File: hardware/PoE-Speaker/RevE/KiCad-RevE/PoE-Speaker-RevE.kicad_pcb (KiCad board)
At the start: 4 copper layers, 210 x 100 mm, 209 parts, among them J1 2250506-1, J2 MX2EDGR-5.08-02P-GN01-Cu-A, J3 MX2EDGR-5.08-02P-GN01-Cu-A, J4 Pin Header 02x07 2.54mm Verti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, J5 Pin Header 01x06 2.54mm Verti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, J6 Pin Header 01x06 2.54mm Verti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, Q1 DMNH6012LK3-13, Q2 DMNH6012LK3-13, Q3 PSMN4R8-100BSE, Q4 PSMN4R8-100BSE, SW1 TS-1088-AR02016, SW2 TS-1088-AR02016, U1 Ag5800, U10 LM5050-2, U11 PCAL6416APW, U12 PC817X2NSZ9F, U13 PC817X2NSZ9F, U14 PC817X2NSZ9F, U15 LTC4365HTS8#TRPBF, U16 TPS26630RGER, U2 ESP32-S3-WROOM-1U-N16R8, U3 W5500, U4 PCM5122PWR, U5 TPA3116D2, U6 LMR33630AQRNXRQ1, U7 TPS62132RGTR, U8 RT9013-33GB, U9 LM5050-2, X2 25MHz

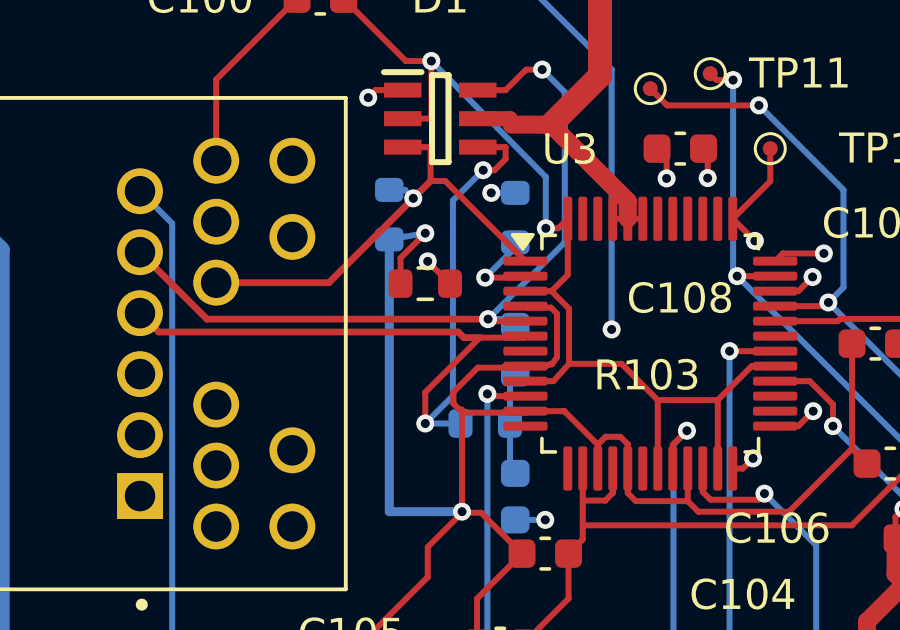
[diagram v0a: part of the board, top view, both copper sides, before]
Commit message: Shorten RX positive branch routing for #1
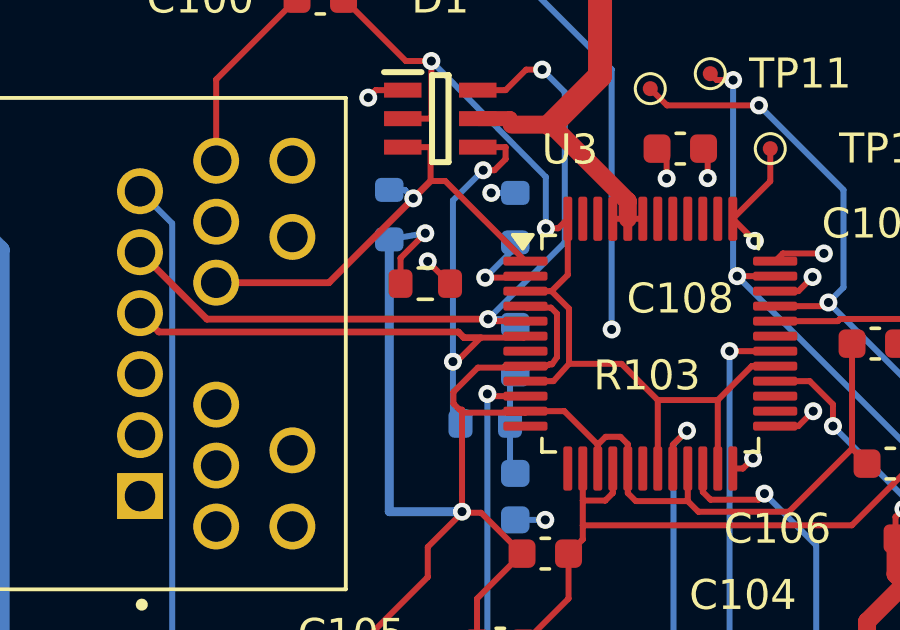
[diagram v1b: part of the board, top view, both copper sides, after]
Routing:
- net ETH_RX_P: track 29.5 -> 25.7 mm
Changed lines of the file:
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@@
 	)
 	(segment
-		(start 117.5 70.6205)
-		(end 119.321 68.7995)
+		(start 119.806 63.2193)
+		(end 119.431 63.2193)
 		(width 0.2)
 		(layer "F.Cu")
@@
 	)
 	(segment
-		(start 119.806 63.2193)
-		(end 119.431 63.2193)
+		(start 119.348 68.7995)
+		(end 118.5475 69.6)
 		(width 0.2)
 		(layer "F.Cu")
@@
 	)
 	(segment
-		(start 120.177 62.45)
-		(end 120.177 62.8482)
+		(start 118.5475 69.6)
+		(end 118.422 69.6)
 		(width 0.2)
 		(layer "F.Cu")
@@
 	)
 	(segment
-		(start 117.5 71.6622)
-		(end 117.5 70.6205)
+		(start 120.177 62.45)
+		(end 120.177 62.8482)
 		(width 0.2)
 		(layer "F.Cu")
@@
 		(end 118.787894 68.7995)
 		(width 0.225806)
-		(layer "F.Cu")
-		(net "ETH_RX_P")
-	)
-	(segment
-		(start 119.321 68.7995)
-		(end 119.348 68.7995)
-		(width 0.2)
 		(layer "F.Cu")
 		(net "ETH_RX_P")
@@
 	)
 	(via
-		(at 117.5 71.6622)
+		(at 118.422 69.6)
 		(size 0.6)
 		(drill 0.3)
@@
 	)
 	(segment
-		(start 117.5 71.6622)
-		(end 118.422 70.74)
-		(width 0.2)
-		(layer "B.Cu")
-		(net "ETH_RX_P")
-	)
-	(segment
-		(start 117.5 71.6622)
+		(start 118.422 71.4092)
 		(end 118.675 71.6622)
 		(width 0.2)
@@
 	)
 	(segment
-		(start 118.422 70.74)
-		(end 118.422 64.2283)
+		(start 118.422 64.2283)
+		(end 118.422 69.6)
 		(width 0.2)
 		(layer "B.Cu")
+		(net "ETH_RX_P")
+	)
+	(segment
+		(start 118.422 69.6)
+		(end 118.422 71.4092)
+		(width 0.2)
+		(layer "B.Cu")

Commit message: Move TX positive ESD branch to front copper for #1
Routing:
- net ETH_TX_P: track 23.8 -> 21.9 mm, vias 2 -> 1
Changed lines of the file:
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@@
+	)
+	(segment
+		(start 114.2 64.174)
+		(end 115.598 62.776)
+		(width 0.225806)
+		(layer "F.Cu")
+		(net "ETH_TX_P")
 	)
 	(segment
@@
 	)
 	(segment
+		(start 111.292 64.174)
+		(end 114.2 64.174)
+		(width 0.225806)
+		(layer "F.Cu")
+		(net "ETH_TX_P")
+	)
+	(segment
 		(start 115.598 60.7999)
 		(end 115.848 60.55)
 		(width 0.2)
+		(layer "F.Cu")
+		(net "ETH_TX_P")
+	)
+	(segment
+		(start 115.598 62.776)
+		(end 115.598 60.7999)
+		(width 0.225806)
+		(layer "F.Cu")
+		(net "ETH_TX_P")
+	)
+	(segment
+		(start 110.53 64.936)
+		(end 111.292 64.174)
+		(width 0.225806)
 		(layer "F.Cu")
 		(net "ETH_TX_P")
@@
 	(via
 		(at 119.497 66.7995)
-		(size 0.6)
-		(drill 0.3)
-		(layers "F.Cu" "B.Cu")
-		(net "ETH_TX_P")
-	)
-	(via
-		(at 115.598 60.7999)
 		(size 0.6)
 		(drill 0.3)
@@
 	)
 	(segment
-		(start 110.53 64.936)
-		(end 109.436 63.8425)
-		(width 0.2)
-		(layer "In2.Cu")
-		(net "ETH_TX_P")
-	)
-	(segment
 		(start 119.436 66.8605)
 		(end 112.454 66.8605)
 		(width 0.2)
 		(layer "In2.Cu")
-		(net "ETH_TX_P")
-	)
-	(segment
-		(start 111.122 60.7999)
-		(end 115.598 60.7999)
-		(width 0.2)
-		(layer "In2.Cu")
-		(net "ETH_TX_P")
-	)
-	(segment
-		(start 109.436 63.8425)
-		(end 109.436 62.4857)
-		(width 0.2)
-		(layer "In2.Cu")
-		(net "ETH_TX_P")
-	)
-	(segment
-		(start 109.436 62.4857)
-		(end 111.122 60.7999)
-		(width 0.2)
-		(layer "In2.Cu")

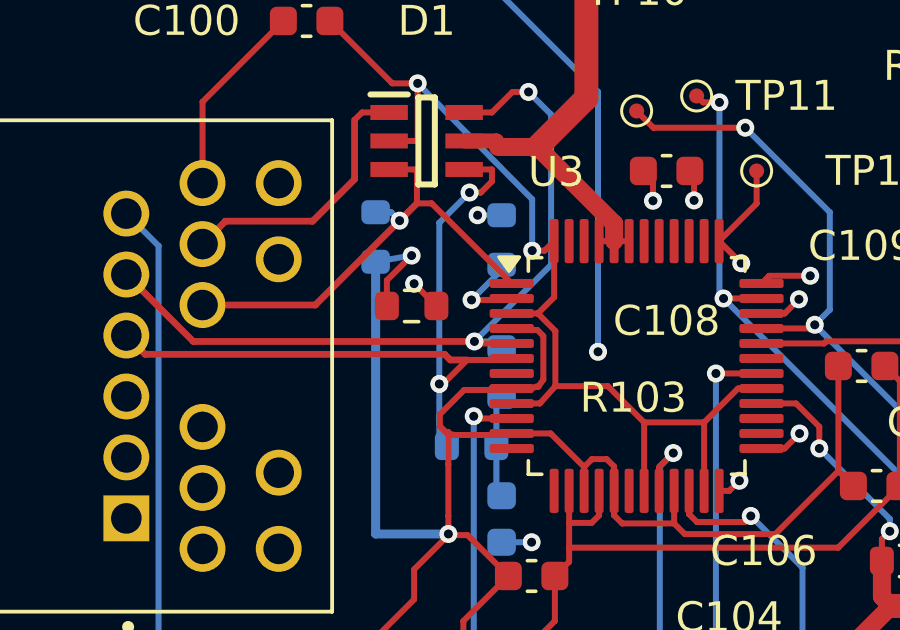
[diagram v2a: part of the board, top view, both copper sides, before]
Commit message: Route shared front-layer TX trunk and relocate termination for #1
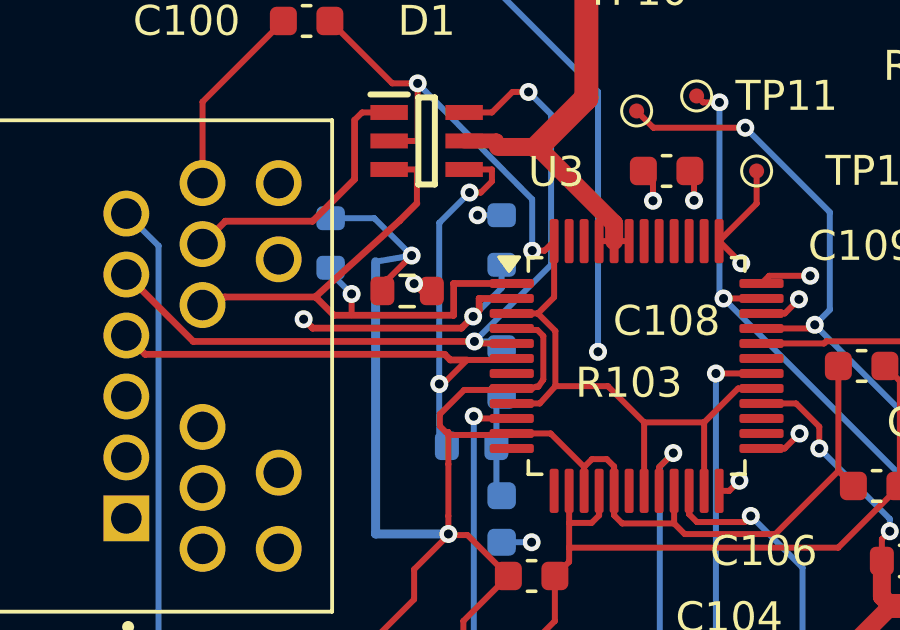
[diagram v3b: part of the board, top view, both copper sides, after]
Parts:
- moved R102 1.51 mm to (114.8, 64.9), turned to 90 degrees
- moved R103 0.52 mm to (117.3, 66.5)
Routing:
- net ETH_TX_N: track 15.8 -> 20.3 mm
- net ETH_3V3A: track 94.7 -> 97.4 mm
- net ETH_TX_P: track 21.9 -> 23.4 mm, vias 1 -> 2
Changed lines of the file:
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@@
 	(footprint "SpeakerRevB:R103_RevB"
 		(layer "F.Cu")
-		(at 117.5 67)
+		(at 117.35 66.5)
 		(descr "Resistor SMD 0603 (1608 Metric), square (rectangular) end terminal, IPC-7351 nominal, (Body size source: IPC-SM-782 page 72, https://www.pcb-3d.com/wordpress/wp-content/uploads/ipc-sm-782a_amendment_1_and_2.pdf)")
 		(tags "resistor")
@@
 	(footprint "SpeakerRevB:R102_RevB"
 		(layer "B.Cu")
-		(at 116.3 64.7 -90)
+		(at 114.8 64.9 90)
 		(descr "Resistor SMD 0603 (1608 Metric), square (rectangular) end terminal, IPC-7351 nominal, (Body size source: IPC-SM-782 page 72, https://www.pcb-3d.com/wordpress/wp-content/uploads/ipc-sm-782a_amendment_1_and_2.pdf)")
 		(tags "resistor")
 		(property "Reference" "R102"
-			(at 0 1.3 90)
+			(at 2.5 1.7 0)
 			(layer "B.SilkS")
 			(effects
@@
 		)
 		(property "Value" "49.9"
-			(at 0 -1.43 90)
+			(at 0 -1.43 270)
 			(layer "B.Fab")
 			(hide yes)
@@
 		)
 		(property "Datasheet" ""
-			(at 0 0 90)
+			(at 0 0 270)
 			(layer "B.Fab")
 			(hide yes)
@@
 		)
 		(property "Description" ""
-			(at 0 0 90)
+			(at 0 0 270)
 			(layer "B.Fab")
 			(hide yes)
@@
 		)
 		(property "KiLib_Generator" "SMD_2terminal_chip_molded"
-			(at 0 0 90)
+			(at 0 0 270)
 			(layer "B.SilkS")
 			(hide yes)
@@
 		(duplicate_pad_numbers_are_jumpers no)
 		(fp_line
-			(start -0.237258 0.5225)
-			(end 0.237258 0.5225)
+			(start -0.237258 -0.5225)
+			(end 0.237258 -0.5225)
 			(stroke
 				(width 0.12)
@@
 		)
 		(fp_line
-			(start -0.237258 -0.5225)
-			(end 0.237258 -0.5225)
+			(start -0.237258 0.5225)
+			(end 0.237258 0.5225)
 			(stroke
 				(width 0.12)
@@
 		)
 		(fp_text user "${REFERENCE}"
-			(at 0 0 90)
+			(at 0 0 270)
 			(layer "B.Fab")
 			(effects
@@
 		)
 		(pad "1" smd roundrect
-			(at -0.825 0 270)
+			(at -0.825 0 90)
 			(size 0.8 0.95)
 			(layers "B.Cu" "B.Mask" "B.Paste")
@@
 		)
 		(pad "2" smd roundrect
-			(at 0.825 0 270)
+			(at 0.825 0 90)
 			(size 0.8 0.95)
 			(layers "B.Cu" "B.Mask" "B.Paste")
@@
 	)
 	(segment
-		(start 116.675 66.1451)
-		(end 116.675 67)
-		(width 0.2)
-		(layer "F.Cu")
-		(net "ETH_3V3A")
-	)
-	(segment
 		(start 117.583 76.781)
 		(end 114.465 79.8985)
@@
 	)
 	(segment
+		(start 116.525 66.2951)
+		(end 116.525 66.5)
+		(width 0.3)
+		(layer "F.Cu")
+		(net "ETH_3V3A")
+	)
+	(segment
 		(start 120 82.776)
 		(end 120.501 82.776)
@@
 	)
 	(segment
+		(start 116.675 66.1451)
+		(end 116.525 66.2951)
+		(width 0.3)
+		(layer "F.Cu")
+		(net "ETH_3V3A")
+	)
+	(segment
 		(start 118.725 72.2722)
 		(end 118.725 74)
@@
 	)
 	(segment
+		(start 114.8 64.075)
+		(end 116.2554 64.075)
+		(width 0.2)
+		(layer "B.Cu")
+		(net "ETH_3V3A")
+	)
+	(segment
+		(start 116.2554 64.075)
+		(end 117.5 65.319599)
+		(width 0.2)
+		(layer "B.Cu")
+		(net "ETH_3V3A")
+	)
+	(segment
 		(start 116.3 65.525)
 		(end 116.3 74.6)
@@
 	)
 	(segment
+		(start 117.582 66.257)
+		(end 117.825 66.5)
+		(width 0.2)
+		(layer "F.Cu")
+		(net "ETH_TX_CT")
+	)
+	(segment
 		(start 110.53 62.904)
 		(end 110.53 60.195)
@@
 	)
 	(segment
-		(start 117.582 66.257)
-		(end 118.325 67)
+		(start 117.825 66.5)
+		(end 118.175 66.5)
 		(width 0.2)
 		(layer "F.Cu")
@@
 	)
 	(segment
-		(start 120.788 66.7995)
-		(end 120.838 66.75)
-		(width 0.2)
-		(layer "F.Cu")
-		(net "ETH_TX_P")
-	)
-	(segment
 		(start 111.292 64.174)
 		(end 114.2 64.174)
@@
 	)
 	(segment
+		(start 119.75 67.15)
+		(end 119.75 66.75)
+		(width 0.225806)
+		(layer "F.Cu")
+		(net "ETH_TX_P")
+	)
+	(segment
+		(start 119.161 67.739)
+		(end 119.55 67.35)
+		(width 0.225806)
+		(layer "F.Cu")
+		(net "ETH_TX_P")
+	)
+	(segment
 		(start 115.598 62.776)
 		(end 115.598 60.7999)
@@
 	)
 	(segment
+		(start 119.75 66.75)
+		(end 120.8375 66.75)
+		(width 0.225806)
+		(layer "F.Cu")
+		(net "ETH_TX_P")
+	)
+	(segment
+		(start 119.55 67.35)
+		(end 119.75 67.15)
+		(width 0.225806)
+		(layer "F.Cu")
+		(net "ETH_TX_P")
+	)
+	(segment
 		(start 110.53 64.936)
 		(end 111.292 64.174)
@@
 	)
 	(segment
-		(start 119.497 66.7995)
-		(end 120.788 66.7995)
-		(width 0.2)
+		(start 113.9 67.44)
+		(end 114.199 67.739)
+		(width 0.225806)
+		(layer "F.Cu")
+		(net "ETH_TX_P")
+	)
+	(segment
+		(start 114.199 67.739)
+		(end 119.161 67.739)
+		(width 0.225806)
 		(layer "F.Cu")
 		(net "ETH_TX_P")
 	)
 	(via
-		(at 119.497 66.7995)
+		(at 119.55 67.35)
+		(size 0.6)
+		(drill 0.3)
+		(layers "F.Cu" "B.Cu")
+		(net "ETH_TX_P")
+	)
+	(via
+		(at 113.9 67.44)
 		(size 0.6)
 		(drill 0.3)
@@
 	)
 	(segment
-		(start 120.5 65.796499)
+		(start 120.5 66.4)
 		(end 120.5 65.625)
 		(width 0.2)
@@
 	)
 	(segment
-		(start 119.497 66.799499)
-		(end 120.5 65.796499)
+		(start 119.55 67.35)
+		(end 120.5 66.4)
 		(width 0.2)
 		(layer "B.Cu")
@@
 	)
 	(segment
-		(start 112.454 66.8605)
-		(end 110.53 64.936)
-		(width 0.2)
+		(start 110.53 64.936)
+		(end 113.034 67.44)
+		(width 0.225806)
 		(layer "In2.Cu")
 		(net "ETH_TX_P")
 	)
 	(segment
-		(start 119.436 66.8605)
-		(end 112.454 66.8605)
-		(width 0.2)
+		(start 113.034 67.44)
+		(end 113.9 67.44)
+		(width 0.225806)
 		(layer "In2.Cu")
 		(net "ETH_TX_P")
 	)
 	(segment
-		(start 119.497 66.7995)
-		(end 119.436 66.8605)
-		(width 0.2)
-		(layer "In2.Cu")
-		(net "ETH_TX_P")
+		(start 118.9 67.31)
+		(end 118.9 66.25)
+		(width 0.225806)
+		(layer "F.Cu")
+		(net "ETH_TX_N")
 	)
 	(segment
-		(start 110.53 66.968)
-		(end 114.288 66.968)
+		(start 118.9 66.25)
+		(end 120.8375 66.25)
 		(width 0.225806)
 		(layer "F.Cu")
@@
 	)
 	(segment
-		(start 117.677 63.5793)
-		(end 118.167 63.5793)
-		(width 0.2)
+		(start 114.288 66.7)
+		(end 114.3 66.7)
+		(width 0.225806)
 		(layer "F.Cu")
 		(net "ETH_TX_N")
@@
 	)
 	(segment
-		(start 118.167 63.5793)
-		(end 120.838 66.25)
+		(start 111.268 66.7)
+		(end 114.288 66.7)
+		(width 0.225806)
+		(layer "F.Cu")
+		(net "ETH_TX_N")
+	)
+	(segment
+		(start 110.53 66.968)
+		(end 111 66.968)
+		(width 0.225806)
+		(layer "F.Cu")
+		(net "ETH_TX_N")
+	)
+	(segment
+		(start 115.5 66.599999)
+		(end 115.5 67.31)
 		(width 0.2)
 		(layer "F.Cu")
@@
 	)
 	(segment
-		(start 114.288 66.968)
+		(start 114.288 66.7)
 		(end 117.1 64.1563)
 		(width 0.225806)
@@
 	)
 	(segment
+		(start 114.3 66.7)
+		(end 114.91 67.31)
+		(width 0.225806)
+		(layer "F.Cu")
+		(net "ETH_TX_N")
+	)
+	(segment
 		(start 116.75 62.45)
 		(end 117.677 62.45)
@@
 	)
 	(segment
+		(start 114.91 67.31)
+		(end 118.9 67.31)
+		(width 0.225806)
+		(layer "F.Cu")
+		(net "ETH_TX_N")
+	)
+	(segment
 		(start 117.1 64.1563)
 		(end 117.677 63.5793)
@@
 		(net "ETH_TX_N")
 	)
+	(segment
+		(start 111 66.968)
+		(end 111.268 66.7)
+		(width 0.225806)
+		(layer "F.Cu")
+		(net "ETH_TX_N")
+	)
 	(via
-		(at 117.1 64.1563)
+		(at 115.5 66.599999)
 		(size 0.6)
 		(drill 0.3)
@@
 	)
 	(segment
-		(start 116.8187 63.875)
-		(end 116.3 63.875)
+		(start 114.8 65.9)
+		(end 114.8 65.724999)
 		(width 0.2)
 		(layer "B.Cu")
@@
 	)
 	(segment
-		(start 117.1 64.1563)
-		(end 116.8187 63.875)
+		(start 115.5 66.599999)
+		(end 114.8 65.9)
 		(width 0.2)
 		(layer "B.Cu")
